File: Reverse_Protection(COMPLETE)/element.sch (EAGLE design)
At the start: 3 parts

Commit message: update board
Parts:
- removed R2: 10k, adafruit:R-US_R0805
- added D1: BZX55, diode:BZX55
- FLIP: value IRFD9120 -> Si7145DP; MPN (none) -> SI7145DP-T1-GE3; OC_NEWARK (none) -> 63R6006
- R1: MPN (none) -> RC0603FR-0710KL; OC_NEWARK (none) -> 68R0049
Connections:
- net N$2: now also D1.A; no longer R2.2
- net N$3: now also D1.C; no longer R2.1
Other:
- note added: "BATTERY_IN"
- note added: "BATTERY_OUT"
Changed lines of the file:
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@@
 </classes>
 <parts>
-<part name="R1" library="adafruit" deviceset="R-US_" device="R0805" value="10k"/>
-<part name="R2" library="adafruit" deviceset="R-US_" device="R0805" value="10k"/>
-<part name="FLIP" library="transistor-small-signal" library_urn="urn:adsk.eagle:library:401" deviceset="IRFD9120" device="" package3d_urn="urn:adsk.eagle:package:29750/1"/>
+<part name="R1" library="adafruit" deviceset="R-US_" device="R0805" value="10k">
+<attribute name="MF" value=""/>
+<attribute name="MPN" value="RC0603FR-0710KL"/>
+<attribute name="OC_NEWARK" value="68R0049"/>
+</part>
+<part name="FLIP" library="transistor-small-signal" library_urn="urn:adsk.eagle:library:401" deviceset="IRFD9120" device="" package3d_urn="urn:adsk.eagle:package:29750/1" value="Si7145DP">
+<attribute name="MF" value=""/>
+<attribute name="MPN" value="SI7145DP-T1-GE3"/>
+<attribute name="OC_NEWARK" value="63R6006"/>
+</part>
 <part name="X_1" library="ngspice-simulation" library_urn="urn:adsk.eagle:library:527439" deviceset="GND" device=""/>
 <part name="X_2" library="ngspice-simulation" library_urn="urn:adsk.eagle:library:527439" deviceset="GND" device=""/>
 <part name="X_3" library="ngspice-simulation" library_urn="urn:adsk.eagle:library:527439" deviceset="GND" device=""/>
+<part name="D1" library="diode" library_urn="urn:adsk.eagle:library:210" deviceset="BZX55" device="" package3d_urn="urn:adsk.eagle:package:43342/1">
+<attribute name="MF" value="FAIRCHILD SEMICONDUCTOR"/>
+<attribute name="MPN" value="BZX79C4V7"/>
+<attribute name="OC_NEWARK" value="18C5987"/>
+</part>
 </parts>
 <sheets>
 <sheet>
 <plain>
+<text x="0" y="-10.16" size="1.778" layer="91">BATTERY_IN</text>
+<text x="58.42" y="-12.7" size="1.778" layer="91">BATTERY_OUT</text>
 </plain>
 <instances>
-<instance part="R1" gate="G$1" x="27.94" y="-17.78" rot="R90"/>
-<instance part="R2" gate="G$1" x="40.64" y="-12.7" rot="R180"/>
-<instance part="FLIP" gate="A" x="27.94" y="-5.08" rot="MR90"/>
+<instance part="R1" gate="G$1" x="27.94" y="-17.78" rot="R90">
+<attribute name="OC_NEWARK" x="27.94" y="-17.78" size="1.778" layer="96" display="off"/>
+<attribute name="MF" x="27.94" y="-17.78" size="1.778" layer="96" display="off"/>
+<attribute name="MPN" x="27.94" y="-17.78" size="1.778" layer="96" display="off"/>
+</instance>
+<instance part="FLIP" gate="A" x="27.94" y="-5.08" rot="MR90">
+<attribute name="OC_NEWARK" x="27.94" y="-5.08" size="1.778" layer="96" display="off"/>
+<attribute name="MF" x="27.94" y="-5.08" size="1.778" layer="96" display="off"/>
+<attribute name="MPN" x="27.94" y="-5.08" size="1.778" layer="96" display="off"/>
+</instance>
 <instance part="X_1" gate="G$1" x="15.24" y="-25.4"/>
 <instance part="X_2" gate="G$1" x="27.94" y="-27.94"/>
 <instance part="X_3" gate="G$1" x="55.88" y="-22.86"/>
+<instance part="D1" gate="1" x="40.64" y="-12.7">
+<attribute name="OC_NEWARK" x="40.64" y="-12.7" size="1.778" layer="96" display="off"/>
+<attribute name="MF" x="40.64" y="-12.7" size="1.778" layer="96" display="off"/>
+<attribute name="MPN" x="40.64" y="-12.7" size="1.778" layer="96" display="off"/>
+</instance>
 </instances>
 <busses>
@@
 <pinref part="R1" gate="G$1" pin="2"/>
 <wire x1="27.94" y1="-10.16" x2="27.94" y2="-12.7" width="0.1524" layer="91"/>
-<pinref part="R2" gate="G$1" pin="2"/>
-<wire x1="27.94" y1="-12.7" x2="35.56" y2="-12.7" width="0.1524" layer="91"/>
+<wire x1="27.94" y1="-12.7" x2="38.1" y2="-12.7" width="0.1524" layer="91"/>
 <junction x="27.94" y="-12.7"/>
+<pinref part="D1" gate="1" pin="A"/>
 </segment>
 </net>
@@
 <wire x1="45.72" y1="-2.54" x2="55.88" y2="-2.54" width="0.1524" layer="91"/>
 <wire x1="55.88" y1="-7.62" x2="55.88" y2="-2.54" width="0.1524" layer="91"/>
-<pinref part="R2" gate="G$1" pin="1"/>
 <wire x1="45.72" y1="-12.7" x2="45.72" y2="-2.54" width="0.1524" layer="91"/>
 <junction x="45.72" y="-2.54"/>
+<pinref part="D1" gate="1" pin="C"/>
+<wire x1="43.18" y1="-12.7" x2="45.72" y2="-12.7" width="0.1524" layer="91"/>
 </segment>
 </net>

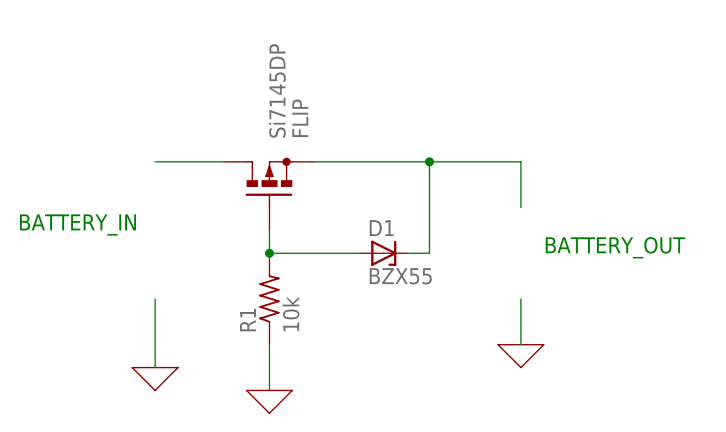
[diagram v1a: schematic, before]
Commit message: update LTspice schematic
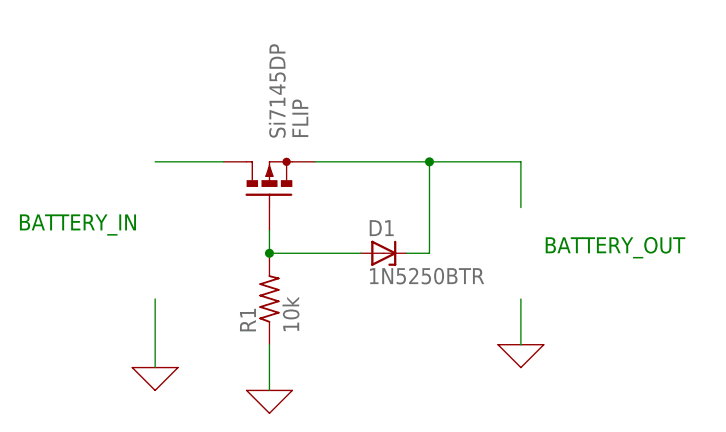
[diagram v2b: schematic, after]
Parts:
- D1: value BZX55 -> 1N5250BTR
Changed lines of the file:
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@@
 <part name="X_2" library="ngspice-simulation" library_urn="urn:adsk.eagle:library:527439" deviceset="GND" device=""/>
 <part name="X_3" library="ngspice-simulation" library_urn="urn:adsk.eagle:library:527439" deviceset="GND" device=""/>
-<part name="D1" library="diode" library_urn="urn:adsk.eagle:library:210" deviceset="BZX55" device="" package3d_urn="urn:adsk.eagle:package:43342/1">
+<part name="D1" library="diode" library_urn="urn:adsk.eagle:library:210" deviceset="BZX55" device="" package3d_urn="urn:adsk.eagle:package:43342/1" value="1N5250BTR">
 <attribute name="MF" value="FAIRCHILD SEMICONDUCTOR"/>
 <attribute name="MPN" value="BZX79C4V7"/>
